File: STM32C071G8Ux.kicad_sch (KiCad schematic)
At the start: 38 parts, among them J1 UJ20-C-H-G-SMT-1-P16-TR, J2 Conn_01x14, J3 Conn_01x14, J4 Conn_ARM_SWD_TagConnect_TC203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, J5 Conn_ARM_JTAG_SWD_10, U1 STM32C071G8Ux, U2 USBLC6-2SC6, U4 TLV75533PDBV

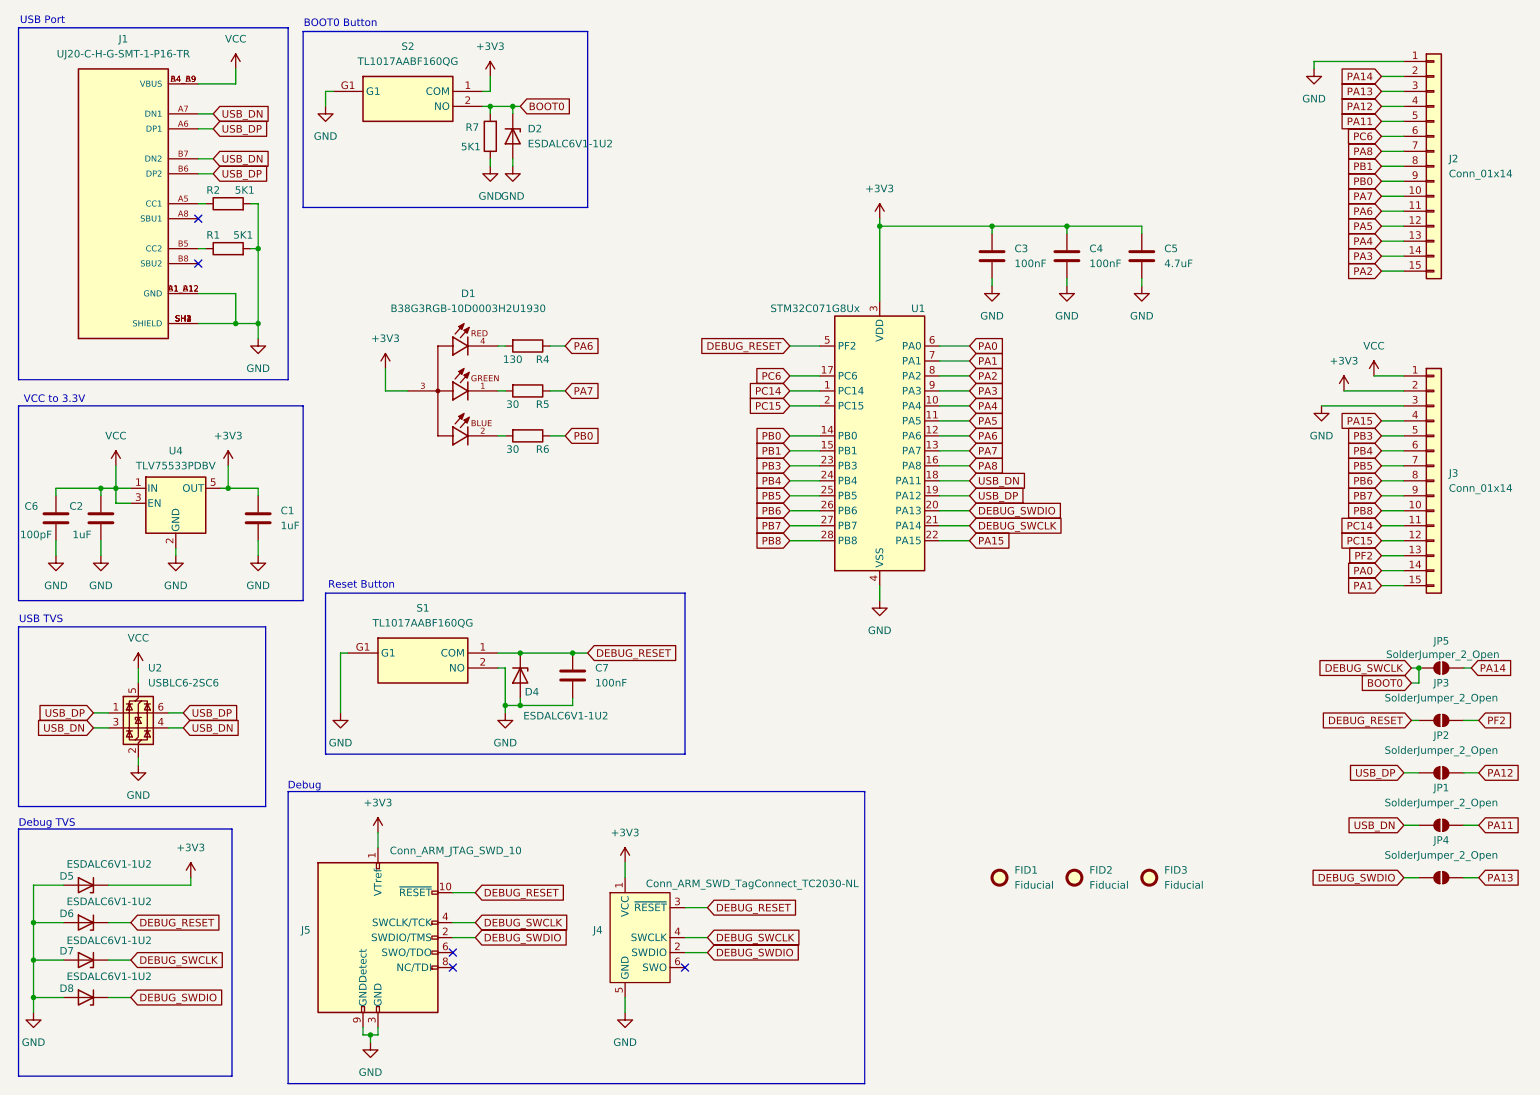
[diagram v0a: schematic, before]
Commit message: fixed some design rules
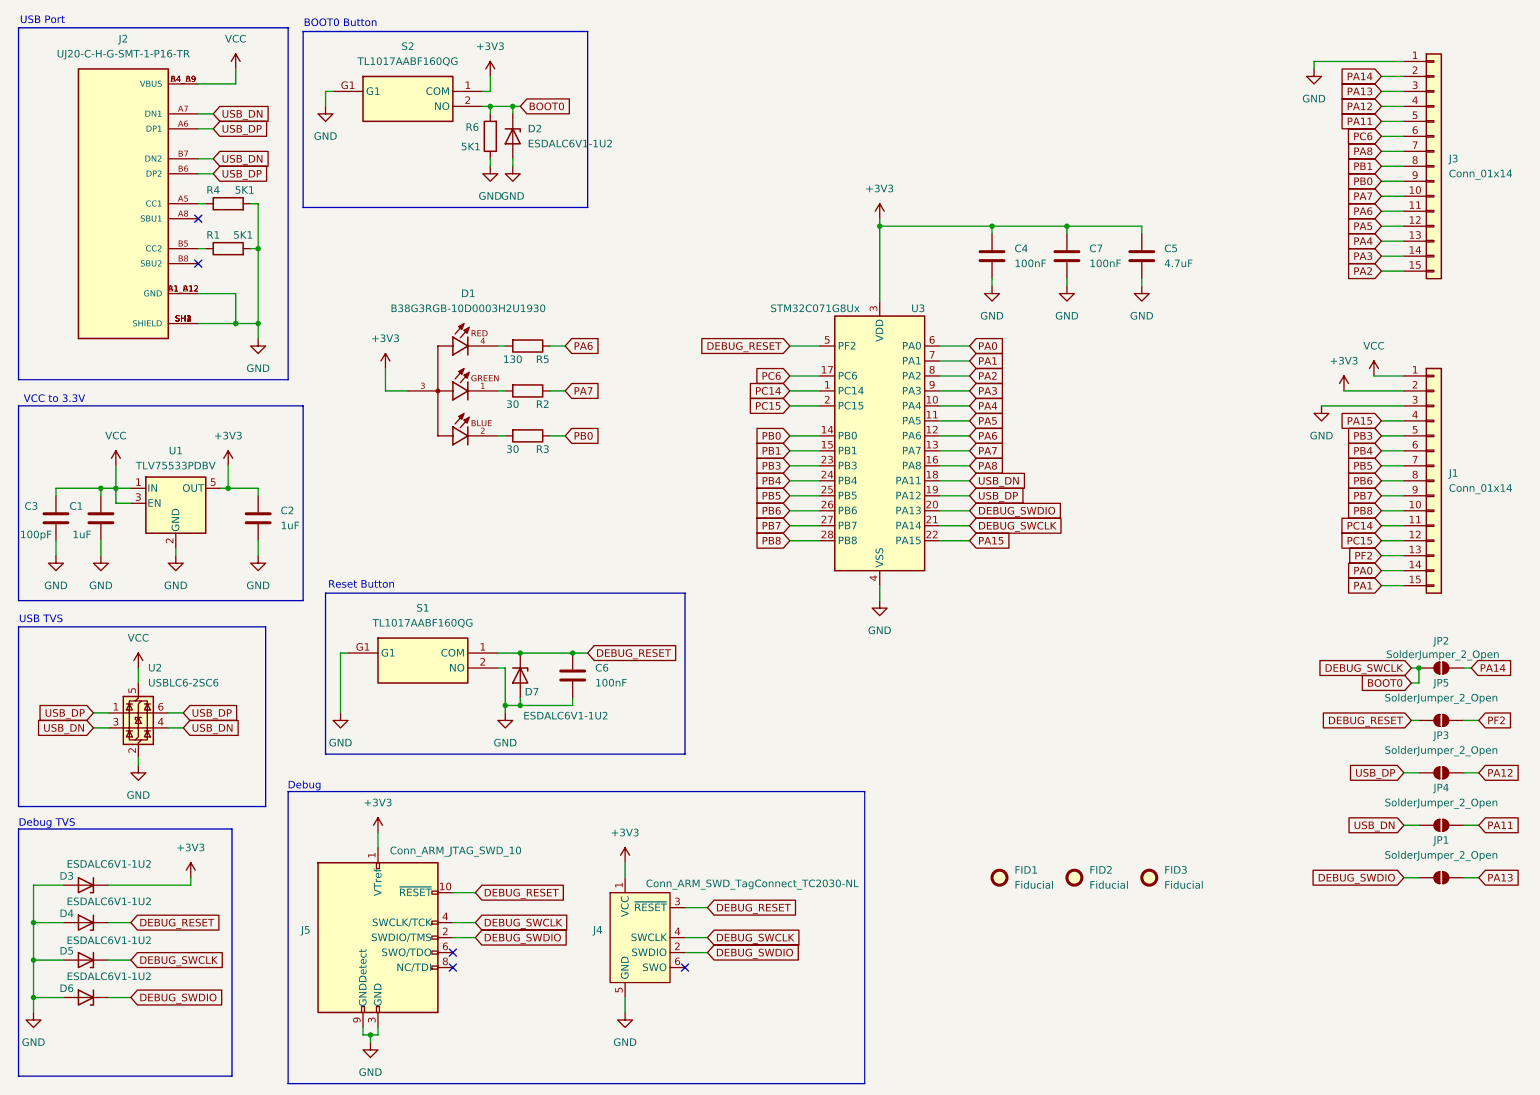
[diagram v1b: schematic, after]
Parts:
- C1: renamed from C2; footprint Capacitor_SMD:C_0402_1005Metric -> footprints:C_0402_1005Metric
- C2: renamed from C1; footprint Capacitor_SMD:C_0402_1005Metric -> footprints:C_0402_1005Metric
- C3: renamed from C6; footprint Capacitor_SMD:C_0402_1005Metric -> footprints:C_0402_1005Metric
- C5: footprint Capacitor_SMD:C_0402_1005Metric -> footprints:C_0402_1005Metric
- C6: renamed from C7; footprint Capacitor_SMD:C_0402_1005Metric -> footprints:C_0402_1005Metric
- C7: renamed from C4; footprint Capacitor_SMD:C_0402_1005Metric -> footprints:C_0402_1005Metric
- JP1: renamed from JP4; footprint Jumper:SolderJumper-2_P1.3mm_Open_TrianglePad1.0x1.5mm -> footprints:SolderJumper-2_P1.3mm_Open_TrianglePad1.0x1.5mm
- JP2: renamed from JP5; footprint Jumper:SolderJumper-2_P1.3mm_Open_TrianglePad1.0x1.5mm -> footprints:SolderJumper-2_P1.3mm_Open_TrianglePad1.0x1.5mm
- JP3: renamed from JP2; footprint Jumper:SolderJumper-2_P1.3mm_Open_TrianglePad1.0x1.5mm -> footprints:SolderJumper-2_P1.3mm_Open_TrianglePad1.0x1.5mm
- JP4: renamed from JP1; footprint Jumper:SolderJumper-2_P1.3mm_Open_TrianglePad1.0x1.5mm -> footprints:SolderJumper-2_P1.3mm_Open_TrianglePad1.0x1.5mm
- JP5: renamed from JP3; footprint Jumper:SolderJumper-2_P1.3mm_Open_TrianglePad1.0x1.5mm -> footprints:SolderJumper-2_P1.3mm_Open_TrianglePad1.0x1.5mm
- renumbered C3 to C4, D5 to D3, D6 to D4, D7 to D5, D8 to D6, D4 to D7, J3 to J1, J1 to J2, J2 to J3, R5 to R2, R6 to R3, R2 to R4, R4 to R5, R7 to R6, U4 to U1, U1 to U3
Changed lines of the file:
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@@
 		(on_board yes)
 		(dnp no)
-		(property "Reference" "C2"
+		(property "Reference" "C1"
 			(at 25.146 97.028 0)
 			(effects
@@
 			)
 		)
-		(property "Footprint" "Capacitor_SMD:C_0402_1005Metric"
+		(property "Footprint" "footprints:C_0402_1005Metric"
 			(at 31.4452 102.87 0)
 			(effects
@@
 			(project "STM32C071G8Ux"
 				(path "/43830917-f7d7-4d02-b833-0362299cee99"
-					(reference "C2")
+					(reference "C1")
 					(unit 1)
 				)
@@
 		(dnp no)
 		(fields_autoplaced yes)
-		(property "Reference" "JP4"
+		(property "Reference" "JP1"
 			(at 257.81 153.67 0)
 			(effects
@@
 			)
 		)
-		(property "Footprint" "Jumper:SolderJumper-2_P1.3mm_Open_TrianglePad1.0x1.5mm"
+		(property "Footprint" "footprints:SolderJumper-2_P1.3mm_Open_TrianglePad1.0x1.5mm"
 			(at 257.81 160.02 0)
 			(effects
@@
 			(project "STM32C071G8Ux"
 				(path "/43830917-f7d7-4d02-b833-0362299cee99"
-					(reference "JP4")
+					(reference "JP1")
 					(unit 1)
 				)
@@
 		(dnp no)
 		(fields_autoplaced yes)
-		(property "Reference" "C4"
+		(property "Reference" "C7"
 			(at 198.12 53.3399 0)
 			(effects
@@
 			)
 		)
-		(property "Footprint" "Capacitor_SMD:C_0402_1005Metric"
+		(property "Footprint" "footprints:C_0402_1005Metric"
 			(at 195.2752 58.42 0)
 			(effects
@@
 			(project "STM32C071G8Ux"
 				(path "/43830917-f7d7-4d02-b833-0362299cee99"
-					(reference "C4")
+					(reference "C7")
 					(unit 1)
 				)
@@
 		(dnp no)
 		(fields_autoplaced yes)
-		(property "Reference" "U4"
+		(property "Reference" "U1"
 			(at 43.18 87.63 0)
 			(effects
@@
 			(project ""
 				(path "/43830917-f7d7-4d02-b833-0362299cee99"
-					(reference "U4")
+					(reference "U1")
 					(unit 1)
 				)
@@
 		(on_board yes)
 		(dnp no)
-		(property "Reference" "C6"
+		(property "Reference" "C3"
 			(at 17.526 97.028 0)
 			(effects
@@
 			)
 		)
-		(property "Footprint" "Capacitor_SMD:C_0402_1005Metric"
+		(property "Footprint" "footprints:C_0402_1005Metric"
 			(at 23.8252 102.87 0)
 			(effects
@@
 			(project "STM32C071G8Ux"
 				(path "/43830917-f7d7-4d02-b833-0362299cee99"
-					(reference "C6")
+					(reference "C3")
 					(unit 1)
 				)
@@
 		(dnp no)
 		(fields_autoplaced yes)
-		(property "Reference" "J1"
+		(property "Reference" "J2"
 			(at 34.29 17.78 0)
 			(effects
@@
 			(project ""
 				(path "/43830917-f7d7-4d02-b833-0362299cee99"
-					(reference "J1")
+					(reference "J2")
 					(unit 1)
 				)
@@
 		(on_board yes)
 		(dnp no)
-		(property "Reference" "U1"
+		(property "Reference" "U3"
 			(at 167.894 63.5 0)
 			(effects
@@
 			(project ""
 				(path "/43830917-f7d7-4d02-b833-0362299cee99"
-					(reference "U1")
+					(reference "U3")
 					(unit 1)
 				)
@@
 		(dnp no)
 		(fields_autoplaced yes)
-		(property "Reference" "J2"
+		(property "Reference" "J3"
 			(at 259.08 38.0999 0)
 			(effects
@@
 			(project ""
 				(path "/43830917-f7d7-4d02-b833-0362299cee99"
-					(reference "J2")
+					(reference "J3")
 					(unit 1)
 				)
@@
 		(dnp no)
 		(fields_autoplaced yes)
-		(property "Reference" "J3"
+		(property "Reference" "J1"
 			(at 259.08 91.4399 0)
 			(effects
@@
 			(project "STM32C071G8Ux"
 				(path "/43830917-f7d7-4d02-b833-0362299cee99"
-					(reference "J3")
+					(reference "J1")
 					(unit 1)
 				)
@@
 		(dnp no)
 		(fields_autoplaced yes)
-		(property "Reference" "JP2"
+		(property "Reference" "JP3"
 			(at 257.81 135.89 0)
 			(effects
@@
 			)
 		)
-		(property "Footprint" "Jumper:SolderJumper-2_P1.3mm_Open_TrianglePad1.0x1.5mm"
+		(property "Footprint" "footprints:SolderJumper-2_P1.3mm_Open_TrianglePad1.0x1.5mm"
 			(at 257.81 142.24 0)
 			(effects
@@
 			(project "STM32C071G8Ux"
 				(path "/43830917-f7d7-4d02-b833-0362299cee99"
-					(reference "JP2")
+					(reference "JP3")
 					(unit 1)
 				)
@@
 		(on_board yes)
 		(dnp no)
-		(property "Reference" "R4"
+		(property "Reference" "R5"
 			(at 105.41 72.136 90)
 			(effects
@@
 			(project "STM32C071G8Ux"
 				(path "/43830917-f7d7-4d02-b833-0362299cee99"
-					(reference "R4")
+					(reference "R5")
 					(unit 1)
 				)
@@
 		(on_board yes)
 		(dnp no)
-		(property "Reference" "D5"
+		(property "Reference" "D3"
 			(at 25.908 159.766 0)
 			(effects
@@
 			(project "STM32C071G8Ux"
 				(path "/43830917-f7d7-4d02-b833-0362299cee99"
-					(reference "D5")
+					(reference "D3")
 					(unit 1)
 				)
@@
 		(on_board yes)
 		(dnp no)
-		(property "Reference" "R7"
+		(property "Reference" "R6"
 			(at 93.472 32.766 0)
 			(effects
@@
 			(project "STM32C071G8Ux"
 				(path "/43830917-f7d7-4d02-b833-0362299cee99"
-					(reference "R7")
+					(reference "R6")
 					(unit 1)
 				)
@@
 		(dnp no)
 		(fields_autoplaced yes)
-		(property "Reference" "C7"
+		(property "Reference" "C6"
 			(at 114.3 124.4599 0)
 			(effects
@@
 			)
 		)
-		(property "Footprint" "Capacitor_SMD:C_0402_1005Metric"
+		(property "Footprint" "footprints:C_0402_1005Metric"
 			(at 111.4552 129.54 0)
 			(effects
@@
 			(project "STM32C071G8Ux"
 				(path "/43830917-f7d7-4d02-b833-0362299cee99"
-					(reference "C7")
+					(reference "C6")
 					(unit 1)
 				)
@@
 		(dnp no)
 		(fields_autoplaced yes)
-		(property "Reference" "JP3"
+		(property "Reference" "JP5"
 			(at 257.81 127 0)
 			(effects
@@
 			)
 		)
-		(property "Footprint" "Jumper:SolderJumper-2_P1.3mm_Open_TrianglePad1.0x1.5mm"
+		(property "Footprint" "footprints:SolderJumper-2_P1.3mm_Open_TrianglePad1.0x1.5mm"
 			(at 257.81 133.35 0)
 			(effects
@@
 			(project "STM32C071G8Ux"
 				(path "/43830917-f7d7-4d02-b833-0362299cee99"
-					(reference "JP3")
+					(reference "JP5")
 					(unit 1)
 				)
@@
 		(on_board yes)
 		(dnp no)
-		(property "Reference" "D8"
+		(property "Reference" "D6"
 			(at 25.908 178.816 0)
 			(effects
@@
 			(project "STM32C071G8Ux"
 				(path "/43830917-f7d7-4d02-b833-0362299cee99"
-					(reference "D8")
+					(reference "D6")
 					(unit 1)
 				)
@@
 		(on_board yes)
 		(dnp no)
-		(property "Reference" "R2"
+		(property "Reference" "R4"
 			(at 49.53 43.434 90)
 			(effects
@@
 			(project "STM32C071G8Ux"
 				(path "/43830917-f7d7-4d02-b833-0362299cee99"
-					(reference "R2")
+					(reference "R4")
 					(unit 1)
 				)
@@
 		(on_board yes)
 		(dnp no)
-		(property "Reference" "D6"
+		(property "Reference" "D4"
 			(at 25.908 166.116 0)
 			(effects
@@
 			(project "STM32C071G8Ux"
 				(path "/43830917-f7d7-4d02-b833-0362299cee99"
-					(reference "D6")
+					(reference "D4")
 					(unit 1)
 				)
@@
 		(on_board yes)
 		(dnp no)
-		(property "Reference" "D4"
+		(property "Reference" "D7"
 			(at 102.362 128.524 90)
 			(effects
@@
 			(project "STM32C071G8Ux"
 				(path "/43830917-f7d7-4d02-b833-0362299cee99"
-					(reference "D4")
+					(reference "D7")
 					(unit 1)
 				)
@@
 		(on_board yes)
 		(dnp no)
-		(property "Reference" "R6"
+		(property "Reference" "R3"
 			(at 105.41 87.376 90)
 			(effects
@@
 			(project "STM32C071G8Ux"
 				(path "/43830917-f7d7-4d02-b833-0362299cee99"
-					(reference "R6")
+					(reference "R3")
 					(unit 1)
 				)
@@
 			)
 		)
-		(property "Footprint" "Capacitor_SMD:C_0402_1005Metric"
+		(property "Footprint" "footprints:C_0402_1005Metric"
 			(at 207.9752 58.42 0)
 			(effects
@@
 		(dnp no)
 		(fields_autoplaced yes)
-		(property "Reference" "C1"
+		(property "Reference" "C2"
 			(at 60.96 97.7899 0)
 			(effects
@@
 			)
 		)
-		(property "Footprint" "Capacitor_SMD:C_0402_1005Metric"
+		(property "Footprint" "footprints:C_0402_1005Metric"
 			(at 58.1152 102.87 0)
 			(effects
@@
 			(project ""
 				(path "/43830917-f7d7-4d02-b833-0362299cee99"
-					(reference "C1")
+					(reference "C2")
 					(unit 1)
 				)
@@
 		(on_board yes)
 		(dnp no)
-		(property "Reference" "JP5"
+		(property "Reference" "JP2"
 			(at 257.81 119.888 0)
 			(effects
@@
 			)
 		)
-		(property "Footprint" "Jumper:SolderJumper-2_P1.3mm_Open_TrianglePad1.0x1.5mm"
+		(property "Footprint" "footprints:SolderJumper-2_P1.3mm_Open_TrianglePad1.0x1.5mm"
 			(at 257.81 124.46 0)
 			(effects
@@
 			(project "STM32C071G8Ux"
 				(path "/43830917-f7d7-4d02-b833-0362299cee99"
-					(reference "JP5")
+					(reference "JP2")
 					(unit 1)
 				)
@@
 		(on_board yes)
 		(dnp no)
-		(property "Reference" "D7"
+		(property "Reference" "D5"
 			(at 25.908 172.466 0)
 			(effects
@@
 			(project "STM32C071G8Ux"
 				(path "/43830917-f7d7-4d02-b833-0362299cee99"
-					(reference "D7")
+					(reference "D5")
 					(unit 1)
 				)
@@
 		(dnp no)
 		(fields_autoplaced yes)
-		(property "Reference" "C3"
+		(property "Reference" "C4"
 			(at 185.42 53.3399 0)
 			(effects
@@
 			(project "STM32C071G8Ux"
 				(path "/43830917-f7d7-4d02-b833-0362299cee99"
-					(reference "C3")
+					(reference "C4")
 					(unit 1)
 				)
@@
 		(dnp no)
 		(fields_autoplaced yes)
-		(property "Reference" "JP1"
+		(property "Reference" "JP4"
 			(at 257.81 144.78 0)
 			(effects
@@
 			)
 		)
-		(property "Footprint" "Jumper:SolderJumper-2_P1.3mm_Open_TrianglePad1.0x1.5mm"
+		(property "Footprint" "footprints:SolderJumper-2_P1.3mm_Open_TrianglePad1.0x1.5mm"
 			(at 257.81 151.13 0)
 			(effects
@@
 			(project ""
 				(path "/43830917-f7d7-4d02-b833-0362299cee99"
-					(reference "JP1")
+					(reference "JP4")
 					(unit 1)
 				)
@@
 		(on_board yes)
 		(dnp no)
-		(property "Reference" "R5"
+		(property "Reference" "R2"
 			(at 105.41 79.756 90)
 			(effects
@@
 			(project "STM32C071G8Ux"
 				(path "/43830917-f7d7-4d02-b833-0362299cee99"
-					(reference "R5")
+					(reference "R2")
 					(unit 1)
 				)
